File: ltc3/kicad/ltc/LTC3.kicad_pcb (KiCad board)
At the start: 4 copper layers, 202.2 x 150.4 mm, 185 parts, among them J401 RJ45, K401 RELAY_1C, K402 RELAY_1C, P201 MicroFit header, P202 XH header, P204 Pin Head 1x2, P205 Pin Head 1x2, P206 Pin Head 1x2, P301 BeagleBone_Black_Expansion_He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, P302 BeagleBone_Black_Expansion_He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, P303 XH header, P304 XH header, P401 MicroFit header, P402 MicroFit header, P404 MicroFit header, P406 XH header, P408 MicroFit header, P501 MicroFit header, P502 MicroFit header, P601 MicroFit header, Q202 BSS138, Q203 BSS138, Q401 PMV45EN, Q402 PMV45EN, Q402 ZVN4525E6, Q403 PMV45EN, Q404 PMV45EN, Q405 PMV45EN, Q501 PMV45EN, Q502 PMV45EN, Q503 PMV45EN, Q504 PMV45EN, Q601 PMV45EN, Q602 PMV45EN, Q603 PMV45EN, Q604 PMV45EN, SW501 MOMENTARY, SW502 MOMENTARY, SW503 MOMENTARY, SW504 MOMENTARY, SW601 MOMENTARY, SW602 MOMENTARY, SW603 MOMENTARY, SW604 MOMENTARY, U201 PTN78020W, U202 LTC2991, U203 PTN78020H, U204 PTN78020H, U301 CAT24C256, U401 CD74HC14, U402 SN65220DBV, U403 SN74AHC1G08, U404 TLP3542, U501 TLP3542, U502 TLP3542, U503 TLP3542, U504 TLP3542, U601 TLP3542, U602 TLP3542, U603 TLP3542, U604 TLP3542

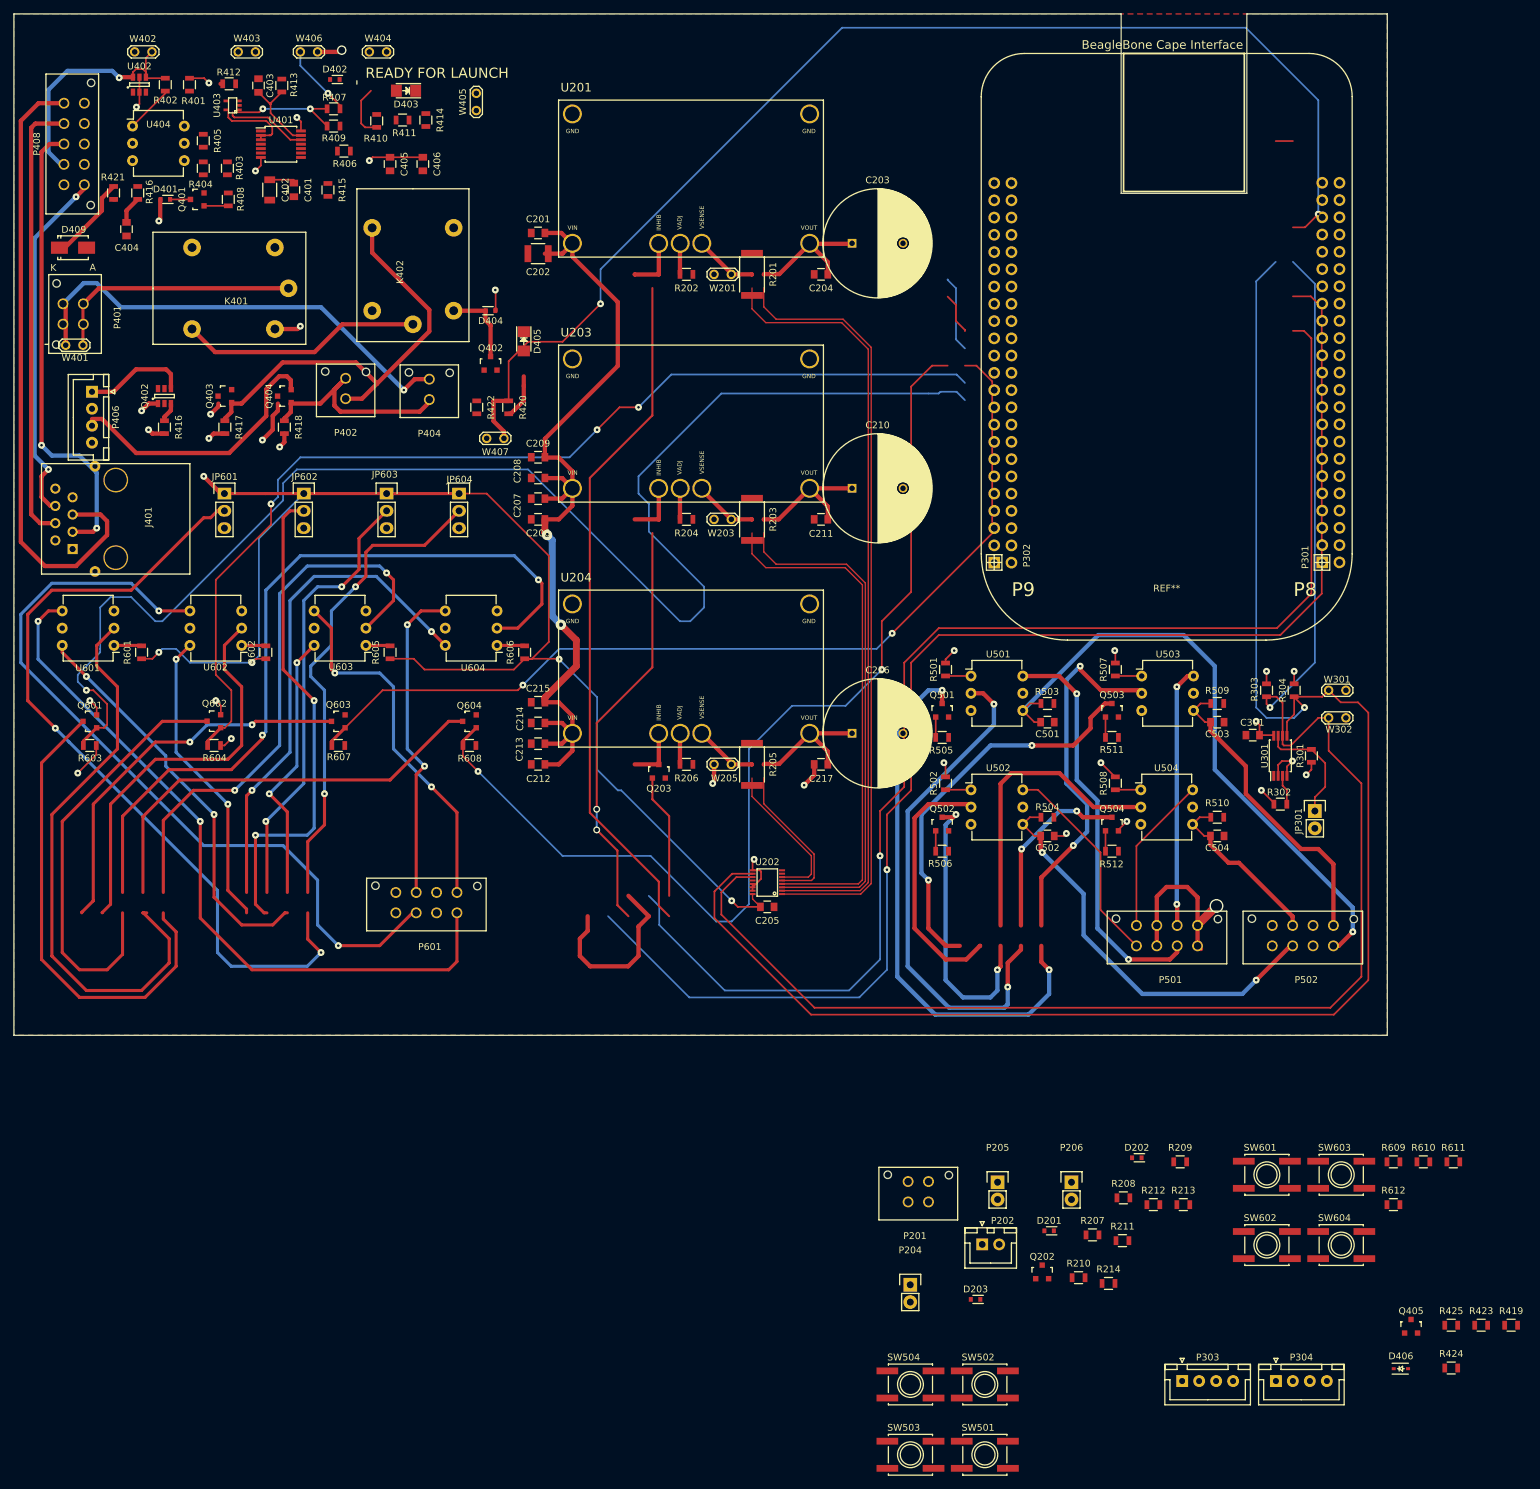
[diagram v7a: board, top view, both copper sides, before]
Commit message: LTC3: LTC Main Board Layout
At long last, 524 Nodes, 205 Nets connected!
Board is passing all DRC runs.  Still needs via stitching and ground plane
flooding, will get to that tomorrow.`
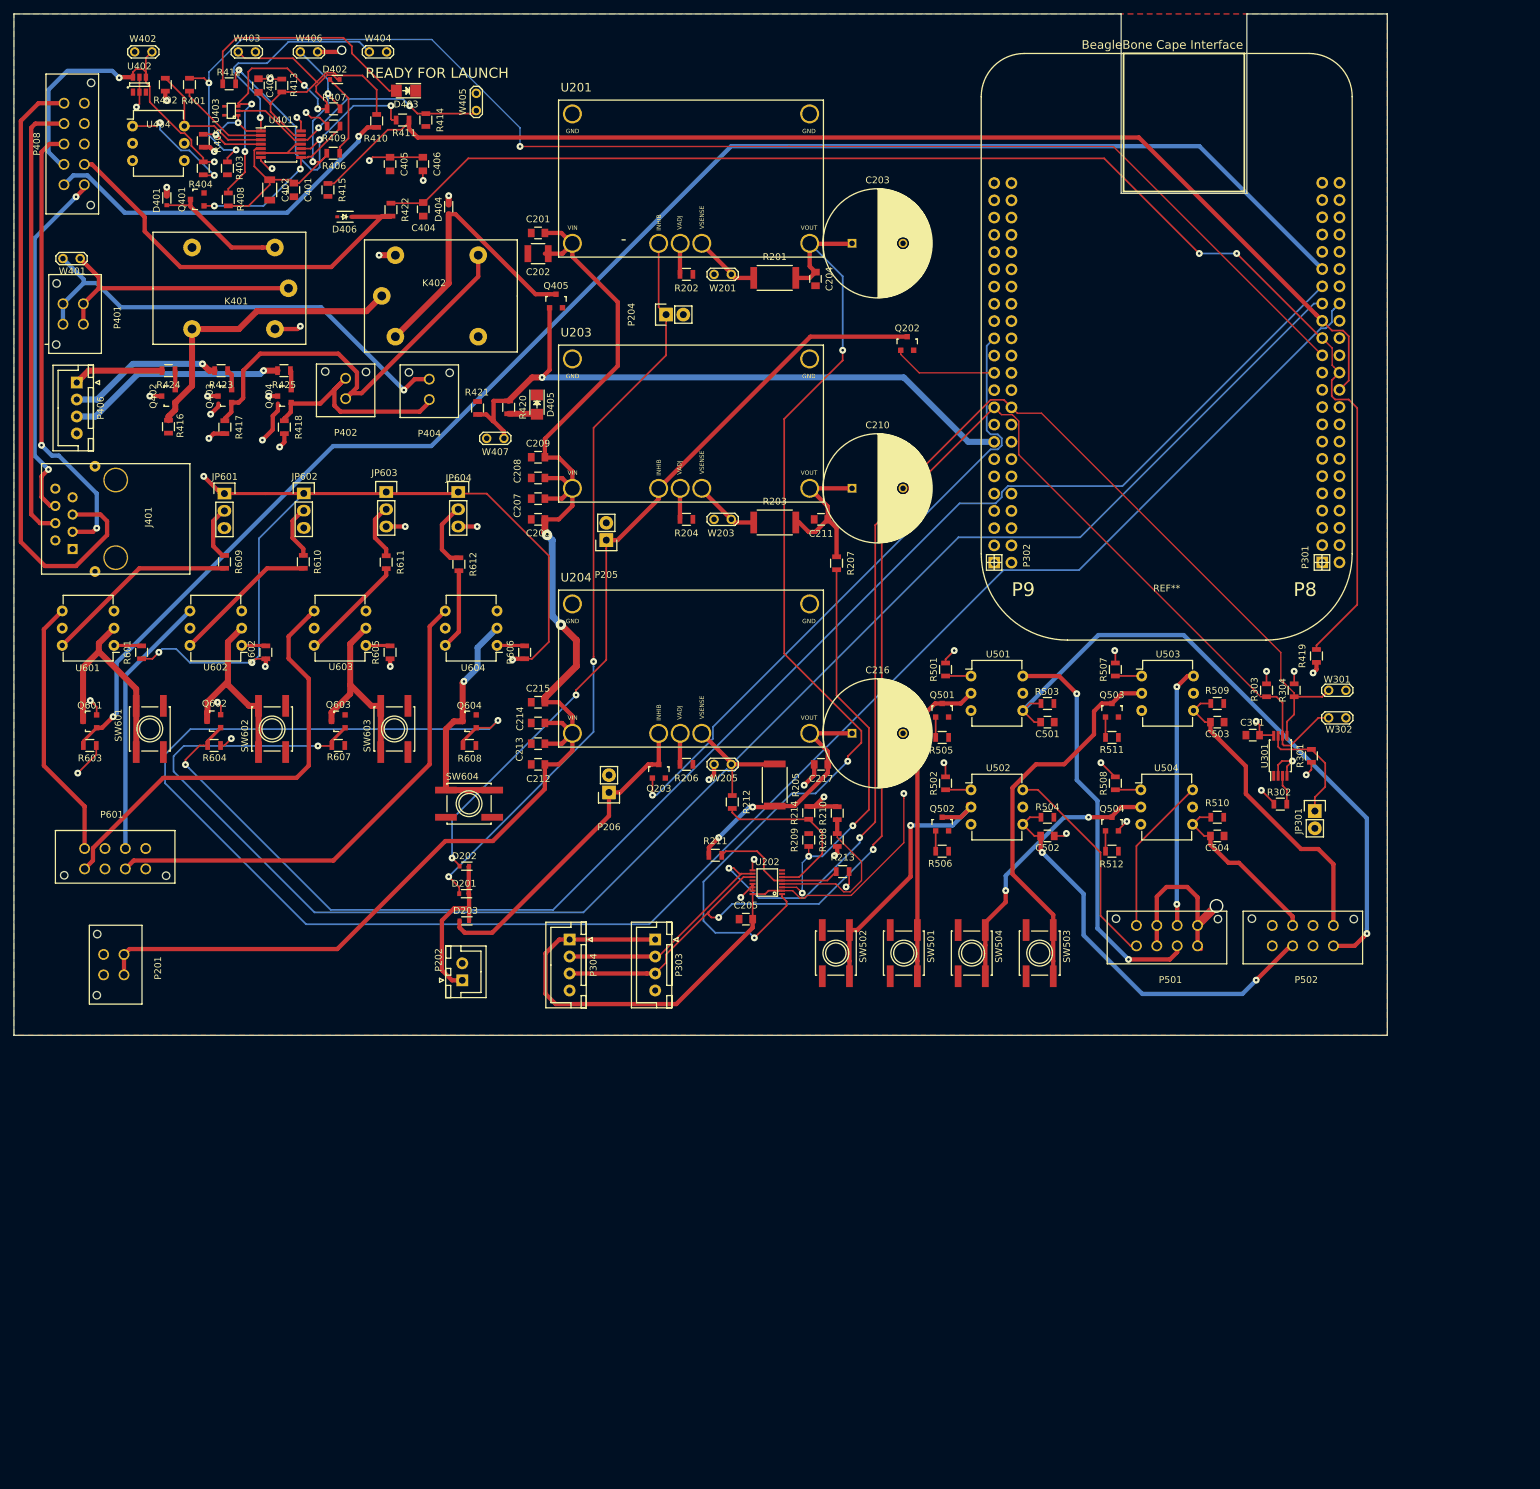
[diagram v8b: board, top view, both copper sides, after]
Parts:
- removed D409: Red, Lg., Diodes_SMD:SMA_Standard
- removed the Q402 at (117.2, 103.0)
- removed the R416 at (117.2, 107.6)
- moved R424 239.2 mm to (117.8, 99.2), turned to 180 degrees
- moved R423 232.7 mm to (125.5, 99.2), turned to 180 degrees
- moved D406 230.1 mm to (143.7, 76.6), turned to 180 degrees
- moved R425 222.0 mm to (134.8, 99.2), turned to 180 degrees
- moved Q405 196.5 mm to (174.8, 89.0)
- moved R609 193.4 mm to (126.0, 127.4), turned to 270 degrees
- moved R610 187.1 mm to (137.6, 127.4), turned to 270 degrees
- moved R611 180.2 mm to (149.8, 127.5), turned to 270 degrees
- moved SW601 177.1 mm to (115.0, 152.0), turned to 90 degrees
- moved R612 166.8 mm to (160.5, 127.8), turned to 270 degrees
- moved SW602 165.0 mm to (133.0, 152.0), turned to 90 degrees
- moved SW603 154.1 mm to (151.0, 152.0), turned to 90 degrees
- moved P204 147.3 mm to (191.0, 91.0), turned to 90 degrees
- moved SW604 143.9 mm to (162.0, 163.0)
- moved Q202 138.1 mm to (226.5, 95.2)
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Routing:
- net /BeagleBone Black Cape/ROCKET_READYn: track 3.65 -> 207.0 mm, vias 1 -> 3
- net /BeagleBone Black Cape/EXT_PWR_EN_4: track 7.87 -> 203.4 mm, vias 0 -> 2
- net /BeagleBone Black Cape/12V_ENn: track 206.1 -> 15.5 mm, vias 1 -> 0
- net (no net): track 198.2 -> 8.37 mm, vias 4 -> 2
- net /BeagleBone Black Cape/BQ_EEPROM: track 11.2 -> 176.7 mm
- net Net-(Q604-Pad3): track 178.2 -> 34.5 mm, vias 2 -> 1
- net /BeagleBone Black Cape/EXT_TRG_EN_4: track 155.6 -> 282.7 mm, vias 2 -> 1
- net Net-(Q601-Pad3): track 155.5 -> 32.7 mm
- net /BeagleBone Black Cape/19V_ENn: track 211.8 -> 94.0 mm
- net Net-(JP601-Pad2): track 120.2 -> 8.20 mm, vias 2 -> 0
- net Net-(Q603-Pad3): track 139.6 -> 28.4 mm, vias 4 -> 0
- net Net-(Q501-Pad3): track 156.3 -> 47.1 mm, vias 4 -> 0
- net /BeagleBone Black Cape/EXT_TRG_EN_3: track 137.9 -> 245.6 mm, vias 2 -> 1
- net Net-(D202-Pad2): track 8.15 -> 115.5 mm, vias 0 -> 2
- net Net-(D201-Pad2): track 8.08 -> 110.1 mm, vias 0 -> 2
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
